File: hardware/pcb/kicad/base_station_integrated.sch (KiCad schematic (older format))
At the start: 2 parts, among them P1 CONN_20X2, U1 PAPILIO_TART

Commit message: Routine backup
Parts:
- added R34, R35, R36, R37: 0, ~, symbol R
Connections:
- net GND: now also R36.1, R37.1
- net CS0: now reaches P1.24 (P24)
- net CS0: now also U1.A9
- new net GND_L: R35.2
- new net GND_PWR: R34.1, R35.1, R36.2, R37.2
- new net GND_T: R34.2
- no-connect marks 47 -> 45

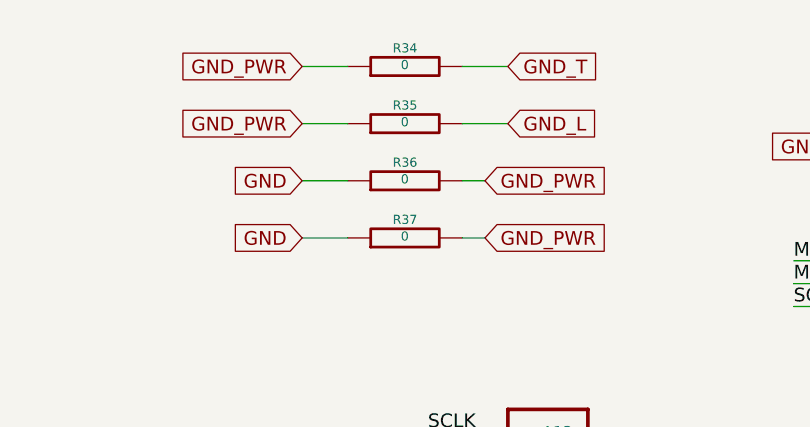
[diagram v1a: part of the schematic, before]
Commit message: New libraries, and board updates
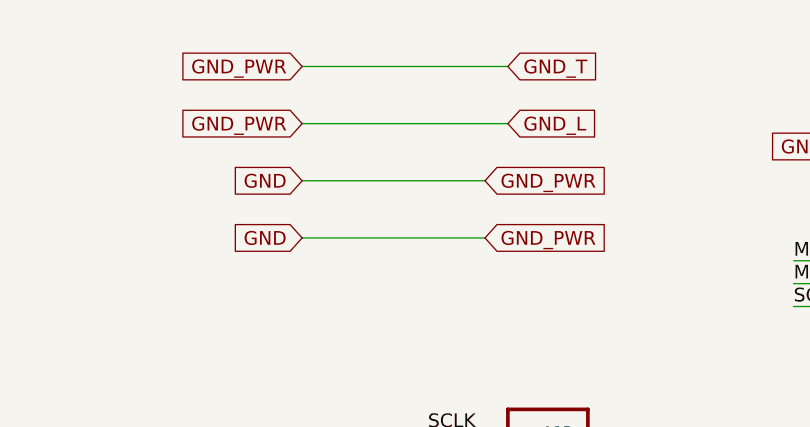
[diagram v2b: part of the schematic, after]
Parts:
- removed R34, R35, R36, R37: 0, ~, symbol R
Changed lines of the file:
@@
 Sheet 1 7
 Title ""
-Date "26 sep 2014"
+Date "6 oct 2014"
 Rev ""
 Comp ""
@@
 Text GLabel 2900 5950 0    60   Input ~ 0
 GND_L
-$Comp
-L R R35
-U 1 1 5424DE9D
-P 7250 1150
-F 0 "R35" V 7330 1150 40  0000 C CNN
-F 1 "0" V 7257 1151 40  0000 C CNN
-F 2 "~" V 7180 1150 30  0000 C CNN
-F 3 "~" H 7250 1150 30  0000 C CNN
-	1    7250 1150
-	0    -1   -1   0
-$EndComp
 Text GLabel 6800 1150 0    60   Input ~ 0
 GND_PWR
 Text GLabel 7700 1150 2    60   Input ~ 0
 GND_L
-$Comp
-L R R34
-U 1 1 5424EBB2
-P 7250 900
-F 0 "R34" V 7330 900 40  0000 C CNN
-F 1 "0" V 7257 901 40  0000 C CNN
-F 2 "~" V 7180 900 30  0000 C CNN
-F 3 "~" H 7250 900 30  0000 C CNN
-	1    7250 900
-	0    -1   -1   0
-$EndComp
 Text GLabel 6800 900  0    60   Input ~ 0
 GND_PWR
@@
 	2900 7150 3000 7150
 Wire Wire Line
-	7500 1150 7700 1150
-Wire Wire Line
-	7000 1150 6800 1150
-Wire Wire Line
-	7500 900  7700 900
-Wire Wire Line
-	7000 900  6800 900
+	7700 1150 6800 1150
+Wire Wire Line
+	7700 900  6800 900
 Text GLabel 6800 1650 0    60   Input ~ 0
 GND
 Text GLabel 7600 1650 2    60   Input ~ 0
 GND_PWR
-$Comp
-L R R36
-U 1 1 54253532
-P 7250 1400
-F 0 "R36" V 7330 1400 40  0000 C CNN
-F 1 "0" V 7257 1401 40  0000 C CNN
-F 2 "~" V 7180 1400 30  0000 C CNN
-F 3 "~" H 7250 1400 30  0000 C CNN
-	1    7250 1400
-	0    -1   -1   0
-$EndComp
-$Comp
-L R R37
-U 1 1 54253541
-P 7250 1650
-F 0 "R37" V 7330 1650 40  0000 C CNN
-F 1 "0" V 7257 1651 40  0000 C CNN
-F 2 "~" V 7180 1650 30  0000 C CNN
-F 3 "~" H 7250 1650 30  0000 C CNN
-	1    7250 1650
-	0    -1   -1   0
-$EndComp
-Wire Wire Line
-	6800 1400 7000 1400
-Wire Wire Line
-	6800 1650 7000 1650
-Wire Wire Line
-	7500 1400 7600 1400
-Wire Wire Line
-	7500 1650 7600 1650
+Wire Wire Line
+	6800 1400 7600 1400
+Wire Wire Line
+	6800 1650 7600 1650
 $EndSCHEMATC

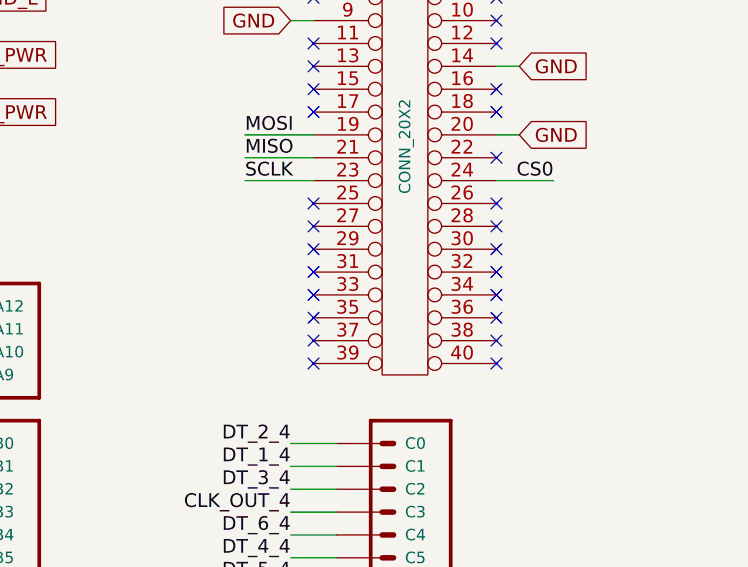
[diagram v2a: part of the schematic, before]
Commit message: Added cover to TCXO. Connected pins on Raspberry Pi to ground
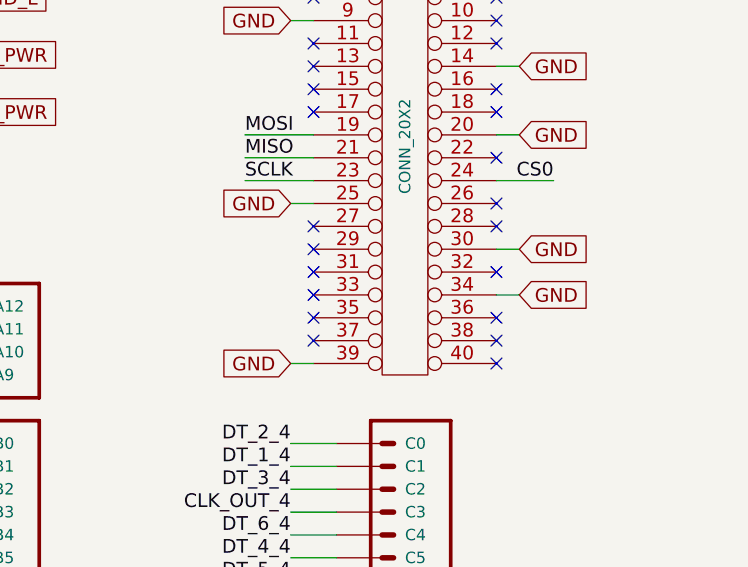
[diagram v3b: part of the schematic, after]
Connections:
- net GND: now also P1.25, P1.30 (P30), P1.34 (P34), P1.39 (P39)
- no-connect marks 45 -> 41
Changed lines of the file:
@@
 Sheet 1 7
 Title ""
-Date "6 oct 2014"
+Date "12 oct 2014"
 Rev ""
 Comp ""
@@
 NoConn ~ 10050 2050
 NoConn ~ 10050 2150
-NoConn ~ 10050 2250
 NoConn ~ 10050 2350
-NoConn ~ 10050 2450
 NoConn ~ 10050 2550
 NoConn ~ 10050 2650
 NoConn ~ 10050 2750
-NoConn ~ 9250 2750
 NoConn ~ 9250 2650
 NoConn ~ 9250 2550
@@
 NoConn ~ 9250 2250
 NoConn ~ 9250 2150
-NoConn ~ 9250 2050
 NoConn ~ 9250 1650
 NoConn ~ 9250 1550
@@
 Wire Wire Line
 	6800 1650 7600 1650
+Text GLabel 9150 2050 0    60   Input ~ 0
+GND
+Text GLabel 10150 2250 2    60   Input ~ 0
+GND
+Text GLabel 10150 2450 2    60   Input ~ 0
+GND
+Text GLabel 9150 2750 0    60   Input ~ 0
+GND
+Wire Wire Line
+	9150 2050 9250 2050
+Wire Wire Line
+	10050 2250 10150 2250
+Wire Wire Line
+	10050 2450 10150 2450
+Wire Wire Line
+	9150 2750 9250 2750
 $EndSCHEMATC
